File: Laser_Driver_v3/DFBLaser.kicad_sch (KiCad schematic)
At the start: 8 parts

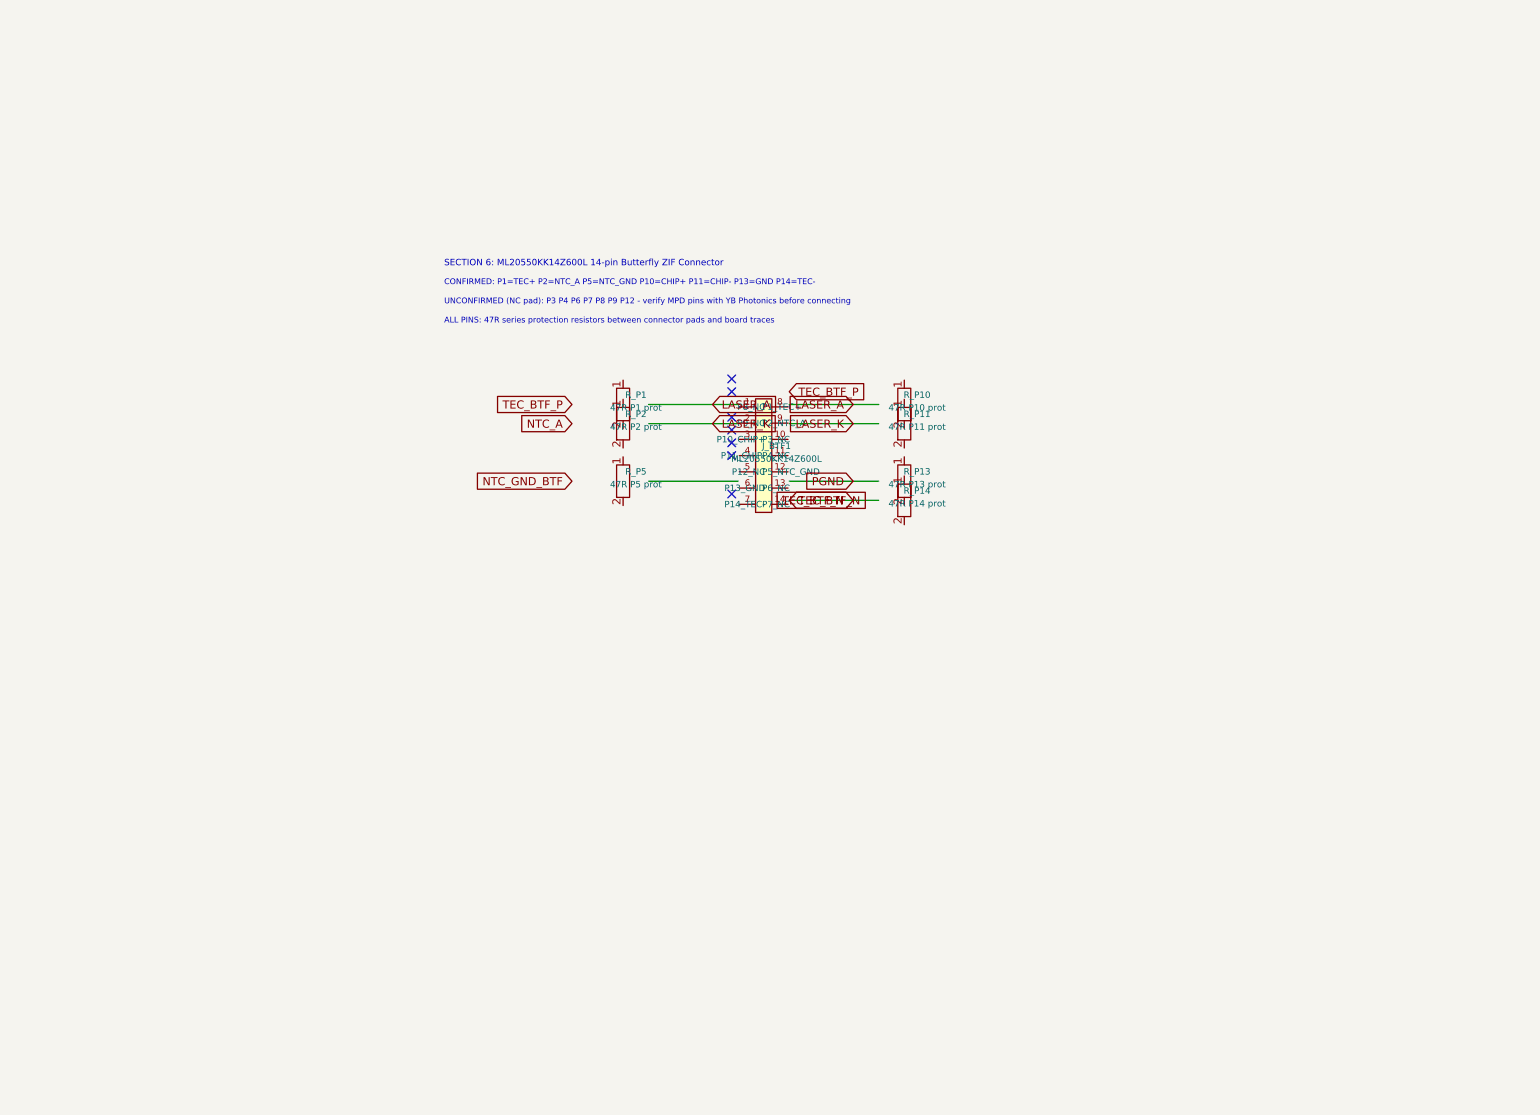
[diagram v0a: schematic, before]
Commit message: Worked on completing Controls and Drivers and CLK.
Laser and TEC drivers and controls now mostly complete.  Added a Clock that runs off an internal 10 MHz or switches to external 10 MHz.  Made minor changes elsewhere.
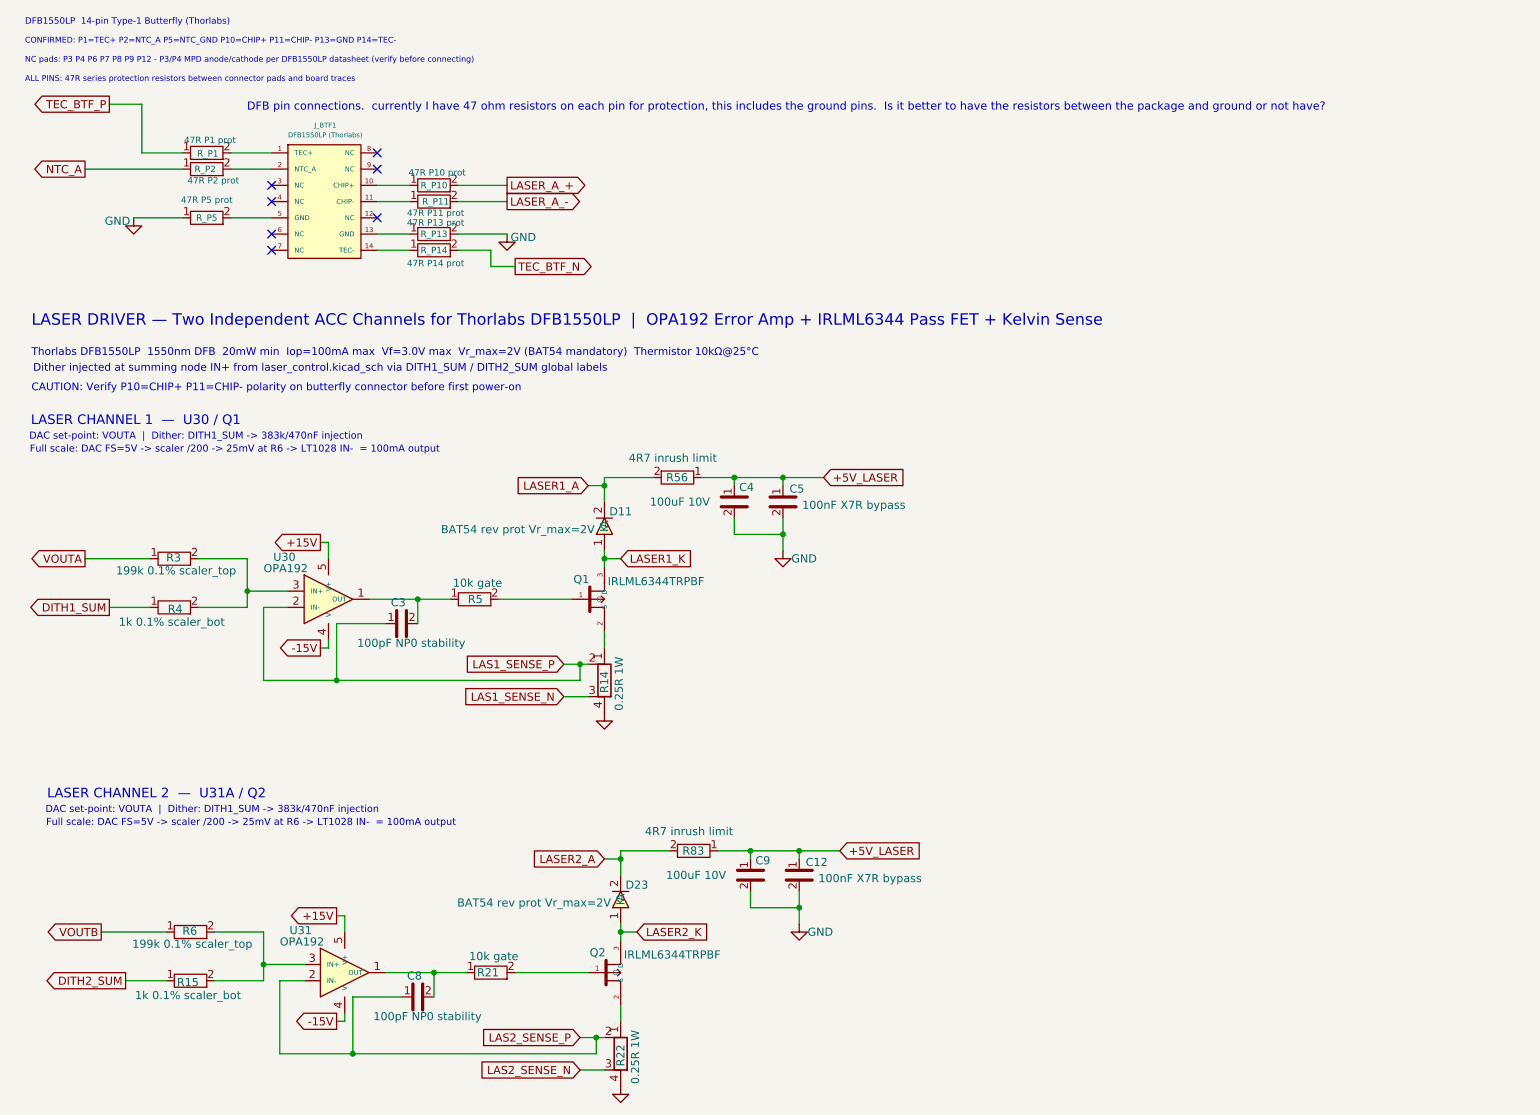
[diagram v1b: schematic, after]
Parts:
- added C12, C5: 100nF X7R bypass, Capacitor_SMD:C_0402_1005Metric, symbol Device:C
- added C3, C8: 100pF NP0 stability, Capacitor_SMD:C_0402_1005Metric, symbol Device:C
- added C4, C9: 100uF 10V, Capacitor_SMD:C_1210_3225Metric, symbol Device:C
- added D11, D23: BAT54 rev prot Vr_max=2V, Diode_SMD:D_SOD-123, symbol Device:D
- added Q1, Q2: IRLML6344TRPBF, Package_TO_SOT_SMD:SOT-23, symbol Transistor_FET:IRLML6344
- added R14, R22: 0.25R 1W, Resistor_SMD:R_Shunt_Vishay_WSKW0612, symbol Device:R_Shunt
- added R15, R4: 1k 0.1% scaler_bot, Resistor_SMD:R_0805_2012Metric, symbol Device:R
- added R21, R5: 10k gate, Resistor_SMD:R_0402_1005Metric, symbol Device:R
- added R3, R6: 199k 0.1% scaler_top, Resistor_SMD:R_0805_2012Metric, symbol Device:R
- added R56, R83: 4R7 inrush limit, Resistor_SMD:R_2512_6332Metric, symbol Device:R
- added U30, U31: OPA192, Package_SO:SOIC-5-6_4.4x3.6mm_P1.27mm, symbol Analog:LT1028
- J_BTF1: value ML20550KK14Z600L -> DFB1550LP (Thorlabs)
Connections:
- net NTC_A: now also R_P2.1
- net TEC_BTF_N: now also R_P14.2
- net TEC_BTF_P: now also R_P1.1
- net at R_P14.1: now also J_BTF1.14 (TEC-)
- net at R_P1.2: now also J_BTF1.1 (TEC+)
- net at R_P10.1: now also J_BTF1.10 (CHIP+)
- net LASER_A_+: now reaches R_P10.2
- net GND: now reaches R_P5.1
- net GND: now also R_P13.2, C12.2, C4.2, C5.2, C9.2, R14.4, R22.4
- net at R_P5.2: now also J_BTF1.5 (GND)
- net at R_P2.2: now also J_BTF1.2 (NTC_A)
- net at J_BTF1.11 (CHIP-): now also R_P11.1
- net at J_BTF1.13 (GND): now also R_P13.1
- net LASER_A_-: now reaches R_P11.2
- new net: C8.2, R21.1, U31.1 (OUT)
- new net: Q2.1 (G), R21.2
- new net: C3.2, R5.1, U30.1 (OUT)
- new net: R3.2, R4.2, U30.3 (IN+)
- new net: Q1.1 (G), R5.2
- new net: Q1.2 (S), R14.1
- new net: Q2.2 (S), R22.1
- new net: R15.2, R6.2, U31.3 (IN+)
- new net +15V: U30.5 (V+), U31.5 (V+)
- new net +5V_LASER: C12.1, C4.1, C5.1, C9.1, R56.1, R83.1
- new net -15V: U30.4 (V-), U31.4 (V-)
- new net DITH1_SUM: R4.1
- new net DITH2_SUM: R15.1
- new net LAS1_SENSE_N: R14.3
- new net LAS1_SENSE_P: C3.1, R14.2, U30.2 (IN-)
- new net LAS2_SENSE_N: R22.3
- new net LAS2_SENSE_P: C8.1, R22.2, U31.2 (IN-)
- new net LASER1_A: D11.2 (K), R56.2
- new net LASER1_K: D11.1 (A), Q1.3 (D)
- new net LASER2_A: D23.2 (K), R83.2
- new net LASER2_K: D23.1 (A), Q2.3 (D)
- new net VOUTA: R3.1
- new net VOUTB: R6.1
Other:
- note added: "CAUTION: Verify P10=CHIP+ P11=CHIP- polarity on butterfly connector before first power-on"
- note added: "DAC set-point: VOUTA | Dither: DITH1_SUM -> 383k/470nF injection"
- note added: "DFB pin connections. currently I have 47 ohm resistors on each pin for protection, this includes the ground pins. Is it better to have the resistors between the package and ground or not have?"
- note added: "DFB1550LP 14-pin Type-1 Butterfly (Thorlabs)"
- note added: "Dither injected at summing node IN+ from laser_control.kicad_sch via DITH1_SUM / DITH2_SUM global labels"
- note added: "Full scale: DAC FS=5V -> scaler /200 -> 25mV at R6 -> LT1028 IN- = 100mA output"
- note added: "LASER CHANNEL 1 — U30 / Q1"
- note added: "LASER CHANNEL 2 — U31A / Q2"
- note added: "LASER DRIVER — Two Independent ACC Channels for Thorlabs DFB1550LP | OPA192 Error Amp + IRLML6344 Pass FET + Kelvin Sense"
- note added: "NC pads: P3 P4 P6 P7 P8 P9 P12 - P3/P4 MPD anode/cathode per DFB1550LP datasheet (verify before connecting)"
- note added: "Thorlabs DFB1550LP 1550nm DFB 20mW min Iop=100mA max Vf=3.0V max Vr_max=2V (BAT54 mandatory) Thermistor 10kΩ@25°C"
- note removed: "SECTION 6: ML20550KK14Z600L 14-pin Butterfly ZIF Connector"
- note removed: "UNCONFIRMED (NC pad): P3 P4 P6 P7 P8 P9 P12 - verify MPD pins with YB Photonics before connecting"

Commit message: Renumbered schematics, corrections, power verified
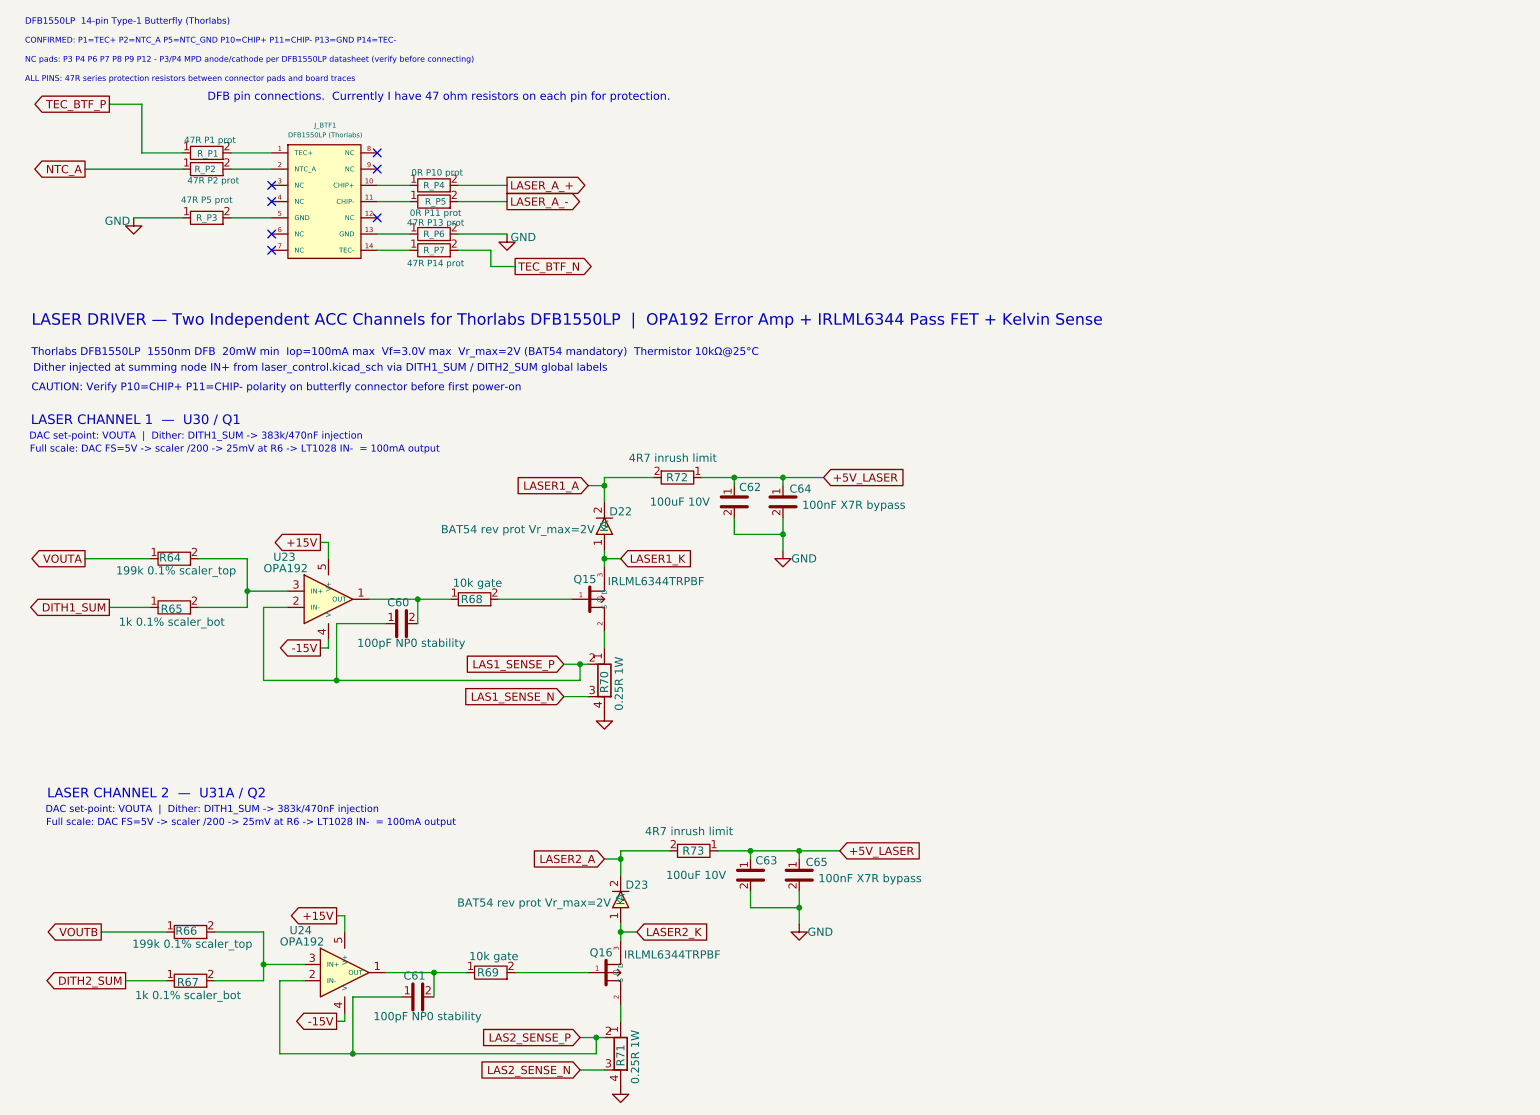
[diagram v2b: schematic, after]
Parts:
- R_P4: renamed from R_P10; value 47R P10 prot -> 0R P10 prot
- R_P5: renamed from R_P11; value 47R P11 prot -> 0R P11 prot
- renumbered C3 to C60, C8 to C61, C4 to C62, C9 to C63, C5 to C64, C12 to C65, D11 to D22, Q1 to Q15, Q2 to Q16, R3 to R64, R4 to R65, R6 to R66, R15 to R67, R5 to R68, R21 to R69, R14 to R70, R22 to R71, R56 to R72, R83 to R73, R_P5 to R_P3, R_P13 to R_P6, R_P14 to R_P7, U30 to U23, U31 to U24
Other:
- note added: "DFB pin connections. Currently I have 47 ohm resistors on each pin for protection."
- note removed: "DFB pin connections. currently I have 47 ohm resistors on each pin for protection, this includes the ground pins. Is it better to have the resistors between the package and ground or not have?"
